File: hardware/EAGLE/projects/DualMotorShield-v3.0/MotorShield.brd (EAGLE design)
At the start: 100 x 80 mm, 82 parts, among them IC2_1_CONN INTEL_BRD, U1 TSR_1-2450

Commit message: progress on DualModorShieldOnRaspberryHat
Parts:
- removed H-BRIDGE2: PWM, SparkFun-Connectors:1X03_NO_SILK
- removed U$10: TEENSY_3.1-3.2_ALL_PINS&PADS, Teensy_3_and_LC_Series_Boards_v1.4:TEENSY_3.0-3.2_ALL_PINS_&_PADS
- added H-BRIDGE0: BLDC0-PWM, SparkFun-Connectors:1X03_NO_SILK
- added X1: RASPI_BOARD_B+_H, raspberrypi_bastelstube_v13:RASPI_BOARD_B+HAT
- H-BRIDGE1: value PWM -> BLDC1-PWM
- SPI_CONN0: value ENCODER -> ENCODER0
- SPI_CONN2: value ENCODER -> ENCODER1
- moved H-BRIDGE1 24.5 mm to (52.4, 49.7), turned to 180 degrees
- renumbered C10 to U0_C5, C11 to V0_C1, C12 to V0_C2, C13 to V0_C3, C14 to V0_C4, C15 to V0_C5, C6 to U0_C1, C7 to U0_C2, C8 to U0_C3, C9 to U0_C4, R10 to V0_R4, R11 to V0_R2, R12 to V0_R1, R5 to U0_R3, R6 to U0_R4, R7 to U0_R2, R8 to U0_R1, R9 to V0_R3, SPI_CONN1 to SPI_CONN0, U$1 to U0_BRIDGE, U$2 to W0_BRIDGE, U$3 to V0_BRIDGE, W_C1 to W0_C1, W_C2 to W0_C2, W_C3 to W0_C3, W_C4 to W0_C4, W_C5 to W0_C5, W_R1 to W0_R1, W_R2 to W0_R2, W_R3 to W0_R3, W_R4 to W0_R4
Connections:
- net U renamed PWM_U0
- net U2 renamed PWN_U1
- net V renamed PWM_V0
- net V2 renamed PWM_V1
- net VI renamed VIN_BATTERY
- net W renamed PWM_W0
- net W2 renamed PWM_W1
- removed net AGND: U$10.AGND
- removed net AREF: U$10.AREF
- removed net CS1: SPI_CONN0.5, U$10.9
- removed net CS2: SPI_CONN2.5, U$10.15/A1
- removed net INH_V: U$10.3, V0_R3.2
- removed net INH_W: U$10.33, W0_R3.2
- removed net IN_U: H-BRIDGE1.3, U0_R4.2
- removed net IN_U2_EX: U$10.21/A7
- removed net IN_U_EX: U$10.5
- removed net IN_V: H-BRIDGE1.2, V0_R4.2
- removed net IN_V2_EX: U$10.22/A8
- removed net IN_V_EX: U$10.6
- removed net IN_W: H-BRIDGE1.1, W0_R4.2
- removed net IN_W2_EX: U$10.23/A9
- removed net IN_W_EX: U$10.10
- removed net IS_U: U$10.26, U0_BRIDGE.6, U0_C1.1, U0_R1.2
- removed net IS_V: U$10.27, V0_BRIDGE.6, V0_C1.1, V0_R1.2
- removed net IS_W: U$10.28, W0_BRIDGE.6, W0_C1.1, W0_R1.2
- removed net MOSI: SPI_CONN0.2, SPI_CONN2.2, U$10.11
- removed net SCK: SPI_CONN0.4, SPI_CONN2.4, U$10.13
- removed net VBAT: U$10.VBAT
- removed net VUSB: U$10.VUSB
- new net 3V3: X1.1
- new net 5V0: X1.2
- new net INH_U0: X1.18
- new net INH_V0: V0_R3.2, X1.16
- new net INH_W0: W0_R3.2, X1.15
- new net IN_U0: H-BRIDGE0.3, U0_R4.2, X1.13
- new net IN_V0: H-BRIDGE0.2, V0_R4.2, X1.12
- new net IN_W0: H-BRIDGE0.1, W0_R4.2, X1.11
- new net IS_U0: U0_BRIDGE.6, U0_C1.1, U0_R1.2, X1.7
- new net IS_V0: V0_BRIDGE.6, V0_C1.1, V0_R1.2, X1.29
- new net IS_W0: W0_BRIDGE.6, W0_C1.1, W0_R1.2, X1.22
- new net SPI_CE0: SPI_CONN0.5, X1.24
- new net SPI_CE1: SPI_CONN2.5, X1.26
- new net SPI_MISO: SPI_CONN0.3, X1.21
- new net SPI_MOSI: SPI_CONN0.2, SPI_CONN2.2, X1.19
- new net SPI_SCLK: SPI_CONN0.4, SPI_CONN2.4, X1.23
- net 3.3V: no longer U$10.3.3V, U$10.3.3V1, U$10.3.3V2
- net GND: now also X1.6; no longer U$10.GND, U$10.GND1, U$10.GND2
- net HALL_U: no longer U$10.20/A6
- net HALL_U2: no longer U$10.14/A0
- net HALL_V: no longer U$10.A10
- net HALL_V2: no longer U$10.16/A2
- net HALL_W: no longer U$10.A11
- net HALL_W2: no longer U$10.17/A3
- net INH_U: no longer U$10.24
- net INH_U2: no longer U$10.2
- net INH_V2: no longer U$10.1
- net INH_W2: no longer U$10.0
- net IN_U2: now also H-BRIDGE1.3; no longer H-BRIDGE2.3
- net IN_V2: now also H-BRIDGE1.2; no longer H-BRIDGE2.2
- net IN_W2: now also H-BRIDGE1.1; no longer H-BRIDGE2.1
- net IS_U2: no longer U$10.31
- net IS_V2: no longer U$10.A13
- net IS_W2: no longer U$10.A12
- net MISO: no longer SPI_CONN0.3, U$10.12
- net SCL0: no longer U$10.19/A5
- net SCL1: no longer U$10.29
- net SDA0: no longer U$10.18/A4
- net SDA1: no longer U$10.30
- net S_PWM_1: no longer U$10.32
- net S_PWM_2: no longer U$10.25
- net VCC: no longer U$10.VIN
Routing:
- net SCK: track 85.8 -> 0.00 mm, vias 2 -> 0
- net SPI_SCLK: track 0.00 -> 85.4 mm, vias 0 -> 2
- net MOSI: track 76.3 -> 0.00 mm, vias 1 -> 0
- net SPI_MOSI: track 0.00 -> 70.9 mm, vias 0 -> 1
- net MISO: track 80.7 -> 13.3 mm, vias 1 -> 0
- net IN_U0: track 0.00 -> 65.3 mm
- net IN_U: track 65.3 -> 0.00 mm
- net INH_V: track 61.2 -> 0.00 mm, vias 1 -> 0
- net INH_V0: track 0.00 -> 59.5 mm, vias 0 -> 1
- net IS_U: track 58.0 -> 0.00 mm, vias 1 -> 0
- net IN_V0: track 0.00 -> 55.7 mm
- net IN_V: track 55.7 -> 0.00 mm
- net IN_W0: track 0.00 -> 54.4 mm, vias 0 -> 2
- net IN_W: track 54.4 -> 0.00 mm, vias 2 -> 0
- net SPI_MISO: track 0.00 -> 53.6 mm, vias 0 -> 1
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
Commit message: Dualboard update
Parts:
- renumbered U$7 to V1_BRIDGE, U$9 to W1_BRIDGE
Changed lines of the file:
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@@
 <attribute name="VALUE" x="61.5696" y="16.002" size="0.6096" layer="28" font="vector" ratio="20" rot="MR0" align="top-center"/>
 </element>
-<element name="U$7" library="ITX007T" package="P-TO263-7-1" package3d_urn="urn:adsk.eagle:package:15313/1" value="" x="58.8264" y="25.908" smashed="yes" rot="R270">
+<element name="V1_BRIDGE" library="ITX007T" package="P-TO263-7-1" package3d_urn="urn:adsk.eagle:package:15313/1" value="" x="58.8264" y="25.908" smashed="yes" rot="R270">
 <attribute name="NAME" x="53.5764" y="31.158" size="1.27" layer="25"/>
 <attribute name="VALUE" x="64.4514" y="30.783" size="1.27" layer="27" rot="R270"/>
@@
 <attribute name="VALUE" x="53.6956" y="51.7144" size="0.6096" layer="27" font="vector" ratio="20" rot="R180"/>
 </element>
-<element name="U$9" library="ITX007T" package="P-TO263-7-1" package3d_urn="urn:adsk.eagle:package:15313/1" value="" x="58.8264" y="38.4048" smashed="yes" rot="R270">
+<element name="W1_BRIDGE" library="ITX007T" package="P-TO263-7-1" package3d_urn="urn:adsk.eagle:package:15313/1" value="" x="58.8264" y="38.4048" smashed="yes" rot="R270">
 <attribute name="NAME" x="53.5764" y="43.6548" size="1.27" layer="25"/>
 <attribute name="VALUE" x="64.4514" y="43.2798" size="1.27" layer="27" rot="R270"/>
@@
 <contactref element="R14" pad="1"/>
 <contactref element="C2" pad="1"/>
-<contactref element="U$7" pad="1" route="any" routetag="G$1.GND"/>
+<contactref element="V1_BRIDGE" pad="1" route="any" routetag="G$1.GND"/>
 <contactref element="R19" pad="1"/>
 <contactref element="C17" pad="2"/>
@@
 <contactref element="R18" pad="1"/>
 <contactref element="C18" pad="1"/>
-<contactref element="U$9" pad="1" route="any" routetag="G$1.GND"/>
+<contactref element="W1_BRIDGE" pad="1" route="any" routetag="G$1.GND"/>
 <contactref element="R23" pad="1"/>
 <contactref element="C22" pad="2"/>
@@
 <contactref element="U0_C3" pad="1"/>
 <contactref element="U0_C4" pad="1"/>
-<contactref element="U$9" pad="7"/>
+<contactref element="W1_BRIDGE" pad="7"/>
 <contactref element="C24" pad="1"/>
 <contactref element="C25" pad="1"/>
@@
 <contactref element="C3" pad="1"/>
 <contactref element="C4" pad="1"/>
-<contactref element="U$7" pad="7"/>
+<contactref element="V1_BRIDGE" pad="7"/>
 <contactref element="C19" pad="1"/>
 <contactref element="C20" pad="1"/>
@@
 </signal>
 <signal name="N$26">
-<contactref element="U$7" pad="3"/>
+<contactref element="V1_BRIDGE" pad="3"/>
 <contactref element="R16" pad="1"/>
 <wire x1="49.6189" y1="27.178" x2="49.6697" y2="27.1272" width="0.254" layer="1"/>
@@
 </signal>
 <signal name="N$27">
-<contactref element="U$7" pad="2"/>
+<contactref element="V1_BRIDGE" pad="2"/>
 <contactref element="R17" pad="1"/>
 <wire x1="49.6189" y1="28.448" x2="52.2224" y2="28.448" width="0.254" layer="1"/>
@@
 </signal>
 <signal name="N$29">
-<contactref element="U$7" pad="5"/>
+<contactref element="V1_BRIDGE" pad="5"/>
 <contactref element="R18" pad="2"/>
 <contactref element="C18" pad="2"/>
@@
 <contactref element="U$8" pad="V"/>
 <contactref element="C20" pad="2"/>
-<contactref element="U$7" pad="4"/>
-<contactref element="U$7" pad="8"/>
+<contactref element="V1_BRIDGE" pad="4"/>
+<contactref element="V1_BRIDGE" pad="8"/>
 <contactref element="C21" pad="2"/>
 <wire x1="60.7196" y1="29.5656" x2="60.7196" y2="28.0416" width="0.254" layer="16"/>
@@
 <signal name="PWM_W1">
 <contactref element="U$8" pad="W"/>
-<contactref element="U$9" pad="4"/>
-<contactref element="U$9" pad="8"/>
+<contactref element="W1_BRIDGE" pad="4"/>
+<contactref element="W1_BRIDGE" pad="8"/>
 <wire x1="60.7196" y1="39.9288" x2="64.9224" y2="39.9288" width="0.254" layer="16"/>
 <via x="64.9224" y="39.9288" extent="1-16" drill="0.35"/>
@@
 </signal>
 <signal name="IS_W2">
-<contactref element="U$9" pad="6"/>
+<contactref element="W1_BRIDGE" pad="6"/>
 <contactref element="R23" pad="2"/>
 <contactref element="C22" pad="1"/>
@@
 </signal>
 <signal name="IS_V2">
-<contactref element="U$7" pad="6"/>
+<contactref element="V1_BRIDGE" pad="6"/>
 <contactref element="R19" pad="2"/>
 <contactref element="C17" pad="1"/>
@@
 </signal>
 <signal name="N$30">
-<contactref element="U$9" pad="3"/>
+<contactref element="W1_BRIDGE" pad="3"/>
 <contactref element="R20" pad="1"/>
 <wire x1="49.6189" y1="39.6748" x2="52.6796" y2="39.6748" width="0.254" layer="1"/>
@@
 </signal>
 <signal name="N$31">
-<contactref element="U$9" pad="2"/>
+<contactref element="W1_BRIDGE" pad="2"/>
 <contactref element="R21" pad="1"/>
 <wire x1="52.7304" y1="40.9448" x2="52.7304" y2="41.7576" width="0.254" layer="1"/>
@@
 </signal>
 <signal name="N$33">
-<contactref element="U$9" pad="5"/>
+<contactref element="W1_BRIDGE" pad="5"/>
 <contactref element="R22" pad="2"/>
 <contactref element="C23" pad="2"/>

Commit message: minor updates on DualMotorShield-v3.0
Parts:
- removed H-BRIDGE0: BLDC0-PWM, SparkFun-Connectors:1X03_NO_SILK
- removed H-BRIDGE1: BLDC1-PWM, SparkFun-Connectors:1X03_NO_SILK
- moved U$4 3.88 mm to (6.92, 26.6)
- renumbered C1 to U1_C1, C17 to V1_C1, C18 to V1_C2, C19 to V1_C3, C2 to U1_D2, C20 to V1_C4, C21 to V1_C5, C22 to W1_C1, C23 to W1_C2, C24 to W1_C3, C25 to W1_C4, C26 to W1_C5, C3 to U1_C3, C4 to U1_C4, C5 to U1_C5, R13 to U1_R4, R14 to U1_R2, R15 to U1_R1, R16 to V1_R3, R17 to V1_R4, R18 to V1_R2, R19 to V1_R1, R20 to W1_R3, R21 to W1_R4, R22 to W1_R2, R23 to W1_R1, R4 to U1_R3, U$6 to U1_BRIDGE
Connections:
- net HALL_U renamed HALL_U0
- net HALL_V renamed HALL_V0
- net HALL_W renamed HALL_W0
- net IS_U2 renamed IS_U1
- removed net 3V3: X1.1
- removed net 5V0: X1.2
- removed net INH_U2: U1_R3.2
- removed net INH_V2: V1_R3.2
- removed net INH_W2: W1_R3.2
- removed net IN_U2: H-BRIDGE1.3, U1_R4.2
- removed net IN_V2: H-BRIDGE1.2, V1_R4.2
- removed net IN_W2: H-BRIDGE1.1, W1_R4.2
- removed net IS_V2: V1_BRIDGE.6, V1_C1.1, V1_R1.2
- removed net IS_W2: W1_BRIDGE.6, W1_C1.1, W1_R1.2
- new net INH_U1: U1_R3.2, X1.37
- new net INH_V1: V1_R3.2, X1.36
- new net INH_W1: W1_R3.2, X1.35
- new net IN_U1: U1_R4.2, X1.33
- new net IN_V1: V1_R4.2, X1.32
- new net IN_W1: W1_R4.2, X1.31
- new net IS_V1: V1_BRIDGE.6, V1_C1.1, V1_R1.2, X1.40
- new net IS_W1: W1_BRIDGE.6, W1_C1.1, W1_R1.2, X1.38
- new net IW_U1: X1.10
- net 3.3V: now also X1.1
- net IN_U0: no longer H-BRIDGE0.3
- net IN_V0: no longer H-BRIDGE0.2
- net IN_W0: no longer H-BRIDGE0.1
- net SCL0: now also X1.5
- net SCL1: now also X1.28
- net SDA0: now also X1.3
- net SDA1: now also X1.27
- net VCC: now also X1.2
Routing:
- net INH_U2: track 66.2 -> 0.00 mm, vias 2 -> 0
- net INH_U1: track 0.00 -> 66.2 mm, vias 0 -> 2
- net IS_V2: track 54.1 -> 0.00 mm, vias 1 -> 0
- net IS_V1: track 0.00 -> 54.1 mm, vias 0 -> 1
- net INH_V2: track 50.0 -> 0.00 mm, vias 1 -> 0
- net INH_V1: track 0.00 -> 50.0 mm, vias 0 -> 1
- net IS_W2: track 39.3 -> 0.00 mm, vias 3 -> 0
- net IS_W1: track 0.00 -> 39.3 mm, vias 0 -> 3
- net IN_U2: track 38.0 -> 0.00 mm, vias 1 -> 0
- net IN_U1: track 0.00 -> 35.8 mm, vias 0 -> 1
- net INH_W2: track 32.9 -> 0.00 mm
- net INH_W1: track 0.00 -> 32.9 mm
- net IN_V2: track 21.6 -> 0.00 mm
- net IN_V1: track 0.00 -> 21.2 mm
- net VIN_BATTERY: track 267.9 -> 259.0 mm
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
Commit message: DualShield update
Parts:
- removed X1: RASPI_BOARD_B+_H, raspberrypi_bastelstube_v13:RASPI_BOARD_B+HAT
- added H-BRIDGE1, H-BRIDGE2: PWM, SparkFun-Connectors:1X03_NO_SILK
- added U$10: TEENSY_3.1-3.2_ALL_PINS&PADS, Teensy_3_and_LC_Series_Boards_v1.4:TEENSY_3.0-3.2_ALL_PINS_&_PADS
- SPI_CONN1: value ENCODER0 -> ENCODER
- SPI_CONN2: value ENCODER1 -> ENCODER
- moved U$4 3.88 mm to (9.67, 29.3)
- renumbered SPI_CONN0 to SPI_CONN1, U0_BRIDGE to U$1, U0_C1 to C6, U0_C2 to C7, U0_C3 to C8, U0_C4 to C9, U0_C5 to C10, U0_R1 to R8, U0_R2 to R7, U0_R3 to R5, U0_R4 to R6, U1_BRIDGE to U$6, U1_C1 to C1, U1_C3 to C3, U1_C4 to C4, U1_C5 to C5, U1_D2 to C2, U1_R1 to R15, U1_R2 to R14, U1_R3 to R4, U1_R4 to R13, V0_BRIDGE to U$3, V0_C1 to C11, V0_C2 to C12, V0_C3 to C13, V0_C4 to C14, V0_C5 to C15, V0_R1 to R12, V0_R2 to R11, V0_R3 to R9, V0_R4 to R10, V1_BRIDGE to U$7, V1_C1 to C17, V1_C2 to C18, V1_C3 to C19, V1_C4 to C20, V1_C5 to C21, V1_R1 to R19, V1_R2 to R18, V1_R3 to R16, V1_R4 to R17, W0_BRIDGE to U$2, W0_C1 to W_C1, W0_C2 to W_C2, W0_C3 to W_C3, W0_C4 to W_C4, W0_C5 to W_C5, W0_R1 to W_R1, W0_R2 to W_R2, W0_R3 to W_R3, W0_R4 to W_R4, W1_BRIDGE to U$9, W1_C1 to C22, W1_C2 to C23, W1_C3 to C24, W1_C4 to C25, W1_C5 to C26, W1_R1 to R23, W1_R2 to R22, W1_R3 to R20, W1_R4 to R21
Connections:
- net PWM_U0 renamed U
- net PWM_V0 renamed V
- net PWM_V1 renamed V2
- net PWM_W0 renamed W
- net PWM_W1 renamed W2
- net PWN_U1 renamed U2
- net VIN_BATTERY renamed VI
- removed net HALL_U0: HALL.2, R2.1
- removed net HALL_V0: HALL.3, R3.1
- removed net HALL_W0: HALL.4, R1.1
- removed net INH_U0: X1.18
- removed net INH_U1: R4.2, X1.37
- removed net INH_V0: R9.2, X1.16
- removed net INH_V1: R16.2, X1.36
- removed net INH_W0: W_R3.2, X1.15
- removed net INH_W1: R20.2, X1.35
- removed net IN_U0: R6.2, X1.13
- removed net IN_U1: R13.2, X1.33
- removed net IN_V0: R10.2, X1.12
- removed net IN_V1: R17.2, X1.32
- removed net IN_W0: W_R4.2, X1.11
- removed net IN_W1: R21.2, X1.31
- removed net IS_U0: C6.1, R8.2, U$1.6, X1.7
- removed net IS_U1: C1.1, R15.2, U$6.6
- removed net IS_V0: C11.1, R12.2, U$3.6, X1.29
- removed net IS_V1: C17.1, R19.2, U$7.6, X1.40
- removed net IS_W0: U$2.6, W_C1.1, W_R1.2, X1.22
- removed net IS_W1: C22.1, R23.2, U$9.6, X1.38
- removed net IW_U1: X1.10
- removed net SPI_CE0: SPI_CONN1.5, X1.24
- removed net SPI_CE1: SPI_CONN2.5, X1.26
- removed net SPI_MISO: SPI_CONN1.3, X1.21
- removed net SPI_MOSI: SPI_CONN1.2, SPI_CONN2.2, X1.19
- removed net SPI_SCLK: SPI_CONN1.4, SPI_CONN2.4, X1.23
- new net AGND: U$10.AGND
- new net AREF: U$10.AREF
- new net CS1: SPI_CONN1.5, U$10.9
- new net CS2: SPI_CONN2.5, U$10.15/A1
- new net HALL_U: HALL.2, R2.1, U$10.20/A6
- new net HALL_V: HALL.3, R3.1, U$10.A10
- new net HALL_W: HALL.4, R1.1, U$10.A11
- new net INH_U2: R4.2, U$10.2
- new net INH_V: R9.2, U$10.3
- new net INH_V2: R16.2, U$10.1
- new net INH_W: U$10.33, W_R3.2
- new net INH_W2: R20.2, U$10.0
- new net IN_U: H-BRIDGE1.3, R6.2
- new net IN_U2: H-BRIDGE2.3, R13.2
- new net IN_U2_EX: U$10.21/A7
- new net IN_U_EX: U$10.5
- new net IN_V: H-BRIDGE1.2, R10.2
- new net IN_V2: H-BRIDGE2.2, R17.2
- new net IN_V2_EX: U$10.22/A8
- new net IN_V_EX: U$10.6
- new net IN_W: H-BRIDGE1.1, W_R4.2
- new net IN_W2: H-BRIDGE2.1, R21.2
- new net IN_W2_EX: U$10.23/A9
- new net IN_W_EX: U$10.10
- new net IS_U: C6.1, R8.2, U$1.6, U$10.26
- new net IS_U2: C1.1, R15.2, U$10.31, U$6.6
- new net IS_V: C11.1, R12.2, U$10.27, U$3.6
- new net IS_V2: C17.1, R19.2, U$10.A13, U$7.6
- new net IS_W: U$10.28, U$2.6, W_C1.1, W_R1.2
- new net IS_W2: C22.1, R23.2, U$10.A12, U$9.6
- new net MOSI: SPI_CONN1.2, SPI_CONN2.2, U$10.11
- new net SCK: SPI_CONN1.4, SPI_CONN2.4, U$10.13
- new net VBAT: U$10.VBAT
- new net VUSB: U$10.VUSB
- net 3.3V: now also U$10.3.3V, U$10.3.3V1, U$10.3.3V2; no longer X1.1
- net GND: now also U$10.GND, U$10.GND1, U$10.GND2; no longer X1.6
- net HALL_U2: now also U$10.14/A0
- net HALL_V2: now also U$10.16/A2
- net HALL_W2: now also U$10.17/A3
- net INH_U: now also U$10.24
- net MISO: now also SPI_CONN1.3, U$10.12
- net SCL0: now also U$10.19/A5; no longer X1.5
- net SCL1: now also U$10.29; no longer X1.28
- net SDA0: now also U$10.18/A4; no longer X1.3
- net SDA1: now also U$10.30; no longer X1.27
- net S_PWM_1: now also U$10.32
- net S_PWM_2: now also U$10.25
- net VCC: now also U$10.VIN; no longer X1.2
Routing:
- net SCK: track 0.00 -> 85.8 mm, vias 0 -> 2
- net SPI_SCLK: track 85.4 -> 0.00 mm, vias 2 -> 0
- net MOSI: track 0.00 -> 76.3 mm, vias 0 -> 1
- net SPI_MOSI: track 70.9 -> 0.00 mm, vias 1 -> 0
- net IS_U2: track 0.00 -> 70.3 mm, vias 0 -> 3
- net IS_U1: track 68.0 -> 0.00 mm, vias 3 -> 0
- net MISO: track 13.3 -> 80.7 mm, vias 0 -> 1
- net INH_U2: track 0.00 -> 66.3 mm, vias 0 -> 2
- net INH_U1: track 66.2 -> 0.00 mm, vias 2 -> 0
- net IN_U0: track 63.6 -> 0.00 mm
- net INH_V: track 0.00 -> 61.2 mm, vias 0 -> 1
- net INH_V0: track 59.5 -> 0.00 mm, vias 1 -> 0
- net IN_U: track 0.00 -> 59.2 mm
- net IS_U: track 0.00 -> 58.0 mm, vias 0 -> 1
- net IN_V: track 0.00 -> 55.7 mm
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
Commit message: spi update
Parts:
- removed U$4, U$8: (no value), 5569-03:5569-003
- added MOTOR0, MOTOR1: PWM, SparkFun-Connectors:1X03_NO_SILK
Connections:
- net 3.3V: now also SPI_CONN1.5, SPI_CONN2.5; no longer SPI_CONN1.1, SPI_CONN2.1
- net CS1: now also SPI_CONN1.1; no longer SPI_CONN1.5
- net CS2: now also SPI_CONN2.1; no longer SPI_CONN2.5
- net MISO: now also SPI_CONN1.4, SPI_CONN2.4; no longer SPI_CONN1.3, SPI_CONN2.3
- net MOSI: now also SPI_CONN1.3, SPI_CONN2.3; no longer SPI_CONN1.2, SPI_CONN2.2
- net SCK: now also SPI_CONN1.2, SPI_CONN2.2; no longer SPI_CONN1.4, SPI_CONN2.4
- net U: now also MOTOR0.1; no longer U$4.W
- net U2: now also MOTOR1.1; no longer U$8.U
- net V: now also MOTOR0.2; no longer U$4.V
- net V2: now also MOTOR1.2; no longer U$8.V
- net W: now also MOTOR0.3; no longer U$4.U
- net W2: now also MOTOR1.3; no longer U$8.W
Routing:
- net V2: track 31.5 -> 38.8 mm
- net U2: track 38.8 -> 46.0 mm
- net V: track 36.1 -> 42.9 mm
- net U: track 41.0 -> 47.6 mm
- net W: track 35.1 -> 41.5 mm
- net W2: track 36.0 -> 41.8 mm
- net SCK: track 85.8 -> 90.5 mm, vias 2 -> 3
- net CS1: track 49.6 -> 53.9 mm
- net CS2: track 36.2 -> 39.7 mm
- net 3.3V: track 101.2 -> 103.3 mm

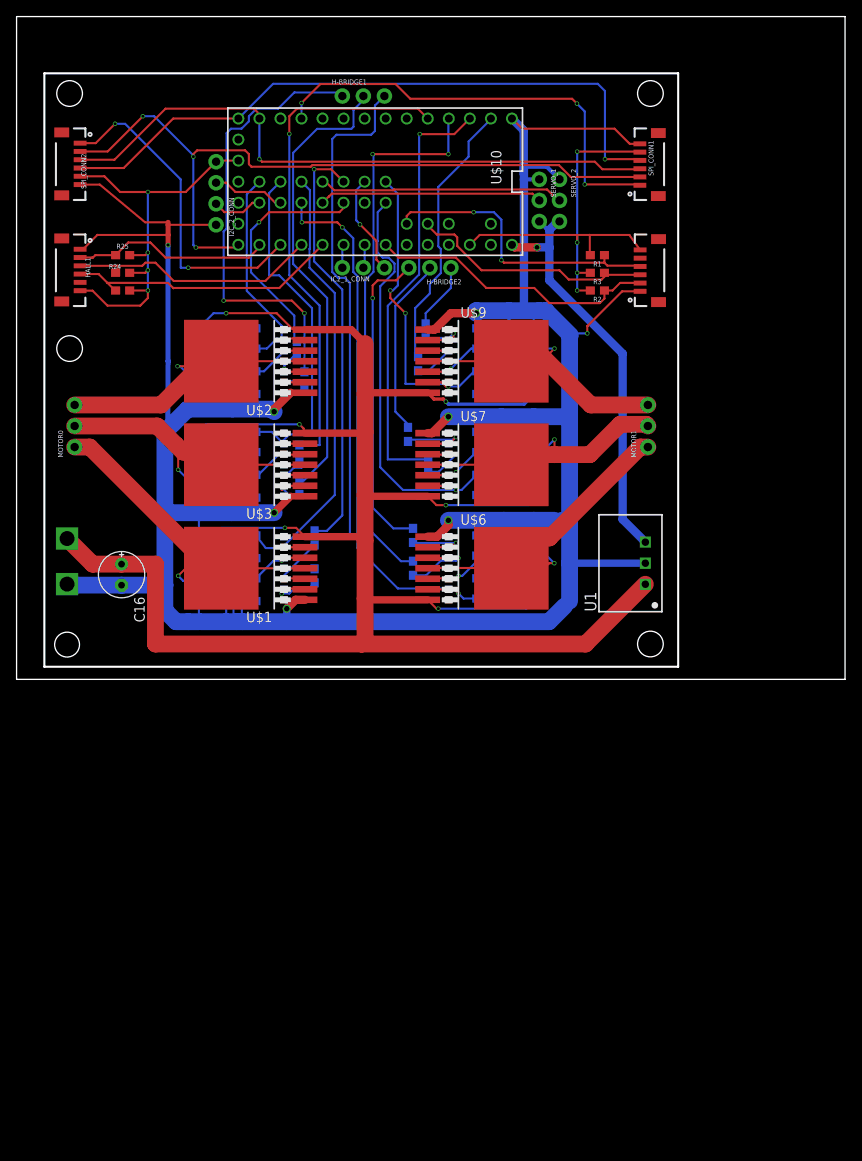
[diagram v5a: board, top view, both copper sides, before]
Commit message: Component renamed
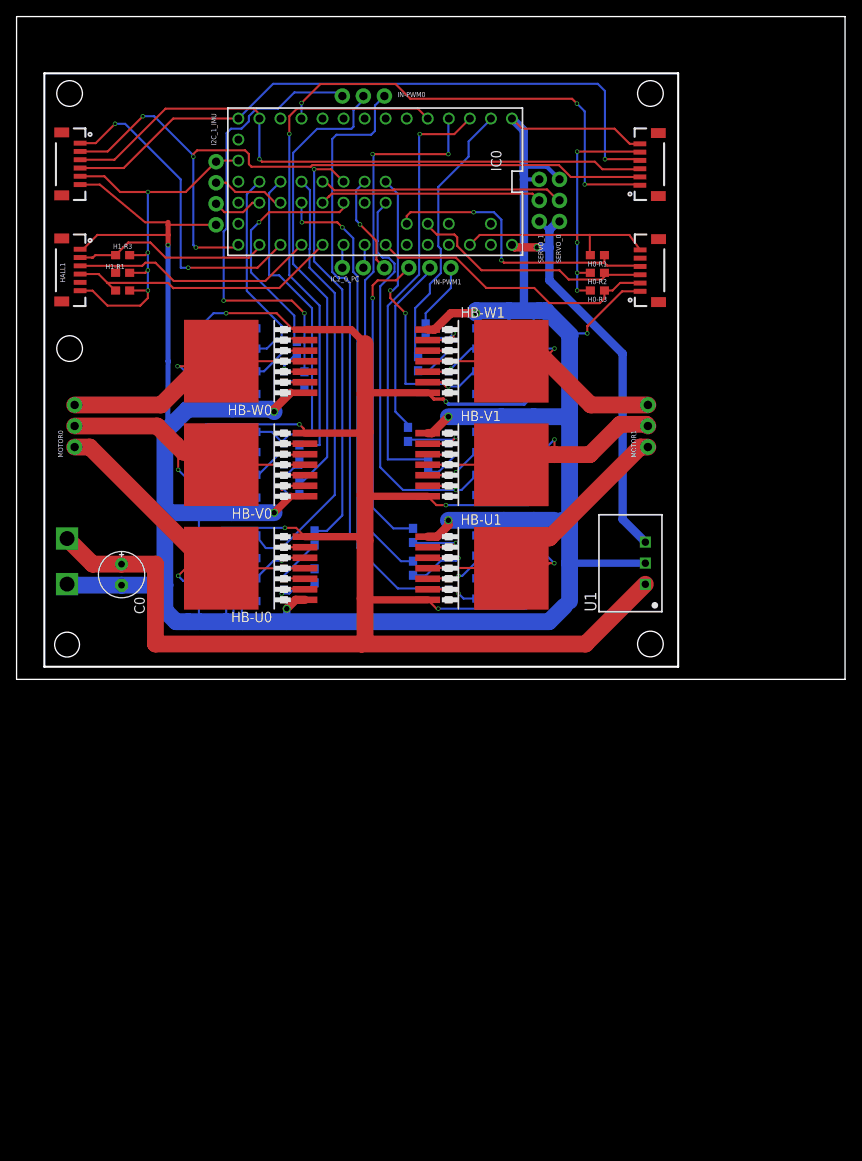
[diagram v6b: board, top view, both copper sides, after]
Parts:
- removed SPI_CONN2: ENCODER, SparkFun-Connectors:1X06-1MM
- added SPI_CONN0: ENCODER0, SparkFun-Connectors:1X06-1MM
- I2C_1_IMU: value IMU_SENS -> JP
- IC2_0_PC: value INTEL_BRD -> JP
- IN-PWM0, IN-PWM1, MOTOR0, MOTOR1: value PWM -> JP
- SERVO_0, SERVO_1: value (none) -> JP
- SPI_CONN1: value ENCODER -> ENCODER1
- moved SPI_CONN1 70.1 mm to (6.40, 62.2), turned to 270 degrees
- renumbered C1 to U1-C1, C10 to U0-C3, C11 to V0-C1, C12 to V0-C2, C13 to V0-C4, C14 to V0-C5, C15 to V0-C3, C16 to C0, C17 to V1-C1, C18 to V1-C2, C19 to V1-C4, C2 to U1-C2, C20 to V1-C5, C21 to V1-C3, C22 to W1-C1, C23 to W1-C2, C24 to W1-C4, C25 to W1-C5, C26 to W1-C3, C3 to U1-C4, C4 to U1-C5, C5 to U1-C3, C6 to U0-C1, C7 to U0-C2, C8 to U0-C4, C9 to U0-C5, H-BRIDGE1 to IN-PWM0, H-BRIDGE2 to IN-PWM1, HALL to HALL0, I2C_2_CONN to I2C_1_IMU, IC2_1_CONN to IC2_0_PC, R1 to H0-R1, R10 to V0-R4, R11 to V0-R2, R12 to V0-R1, R13 to U1-R4, R14 to U1-R2, R15 to U1-R1, R16 to V1-R3, R17 to V1-R4, R18 to V1-R2, R19 to V1-R1, R2 to H0-R3, R20 to W1-R3, R21 to W1-R4, R22 to W1-R2, R23 to W1-R1, R24 to H1-R1, R25 to H1-R3, R26 to H1-R2, R3 to H0-R2, R4 to U1-R3, R5 to U0-R3, R6 to U0-R4, R7 to U0-R2, R8 to U0-R1, R9 to V0-R3, SERVO_2 to SERVO_0, U$1 to HB-U0, U$10 to IC0, U$2 to HB-W0, U$3 to HB-V0, U$6 to HB-U1, U$7 to HB-V1, U$9 to HB-W1, W_C1 to W0-C1, W_C2 to W0-C2, W_C3 to W0-C4, W_C4 to W0-C5, W_C5 to W0-C3, W_R1 to W0-R1, W_R2 to W0-R2, W_R3 to W0-R3, W_R4 to W0-R4
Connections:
- net HALL_U renamed HALL_U0
- net HALL_V renamed HALL_V0
- net HALL_W renamed HALL_W0
- net INH_U renamed INH_U0
- net INH_U2 renamed INH_U1
- net INH_V renamed INH_V0
- net INH_V2 renamed INH_V1
- net INH_W renamed INH_W0
- net INH_W2 renamed INH_W1
- net IN_U renamed IN_U0
- net IN_U2 renamed IN_U1
- net IN_V renamed IN_V0
- net IN_V2 renamed IN_V1
- net IN_W renamed IN_W0
- net IN_W2 renamed IN_W1
- net IS_U renamed IS_U0
- net IS_U2 renamed IS_U1
- net IS_V renamed IS_V0
- net IS_V2 renamed IS_V1
- net IS_W renamed IS_W0
- net IS_W2 renamed IS_W1
- net U renamed U0
- net U2 renamed U1
- net V renamed V0
- net V2 renamed V1
- net W renamed W0
- net W2 renamed W1
- net 3.3V: now also SPI_CONN0.5; no longer SPI_CONN2.5
- net CS1: now also SPI_CONN0.1; no longer SPI_CONN1.1
- net CS2: now also SPI_CONN1.1; no longer SPI_CONN2.1
- net GND: now also SPI_CONN0.6; no longer SPI_CONN2.6
- net MISO: now also SPI_CONN0.4; no longer SPI_CONN2.4
- net MOSI: now also SPI_CONN0.3; no longer SPI_CONN2.3
- net SCK: now also SPI_CONN0.2; no longer SPI_CONN2.2
